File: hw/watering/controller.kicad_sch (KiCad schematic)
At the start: 10 parts, among them U1 ESP32-C6, Y1 40MHz

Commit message: updated power
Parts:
- removed C3: 4u7, Capacitor_SMD:C_0603_1608Metric, symbol Device:C
- added C5, C6, C7, C8: 100n, Capacitor_SMD:C_0603_1608Metric, symbol Device:C
- added SW1, SW2: KMS221GLFS, Button_Switch_SMD:SW_SPST_CK_KMS2xxGP, symbol Switch:SW_Push
- added Y2: 32768Hz, Crystal:Crystal_SMD_3215-2Pin_3.2x1.5mm, symbol Device:Crystal
- AE1: footprint (none) -> RF_Antenna:Texas_SWRA117D_2.4GHz_Left
- C4: value 4u7 -> 100n
- R7, R8: value 5k1 -> 10k
- Y1: footprint (none) -> Crystal:Crystal_SMD_3225-4Pin_3.2x2.5mm
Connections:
- net +3V3: now also C5.1, C6.1, C7.1, C8.1
- net GND: now also C5.2, C6.2, C7.2, C8.2, SW1.1, SW2.1
- net reset: now reaches U1.4 (CHIP_PU)
- net reset: now also SW1.2
- net boot: now reaches U1.6 (GPIO0/XTAL_32K_P/ADC1_CH0)
- net boot: now also SW2.2, Y2.1
- net at U1.7 (GPIO1/XTAL_32K_N/ADC1_CH1): now also Y2.2

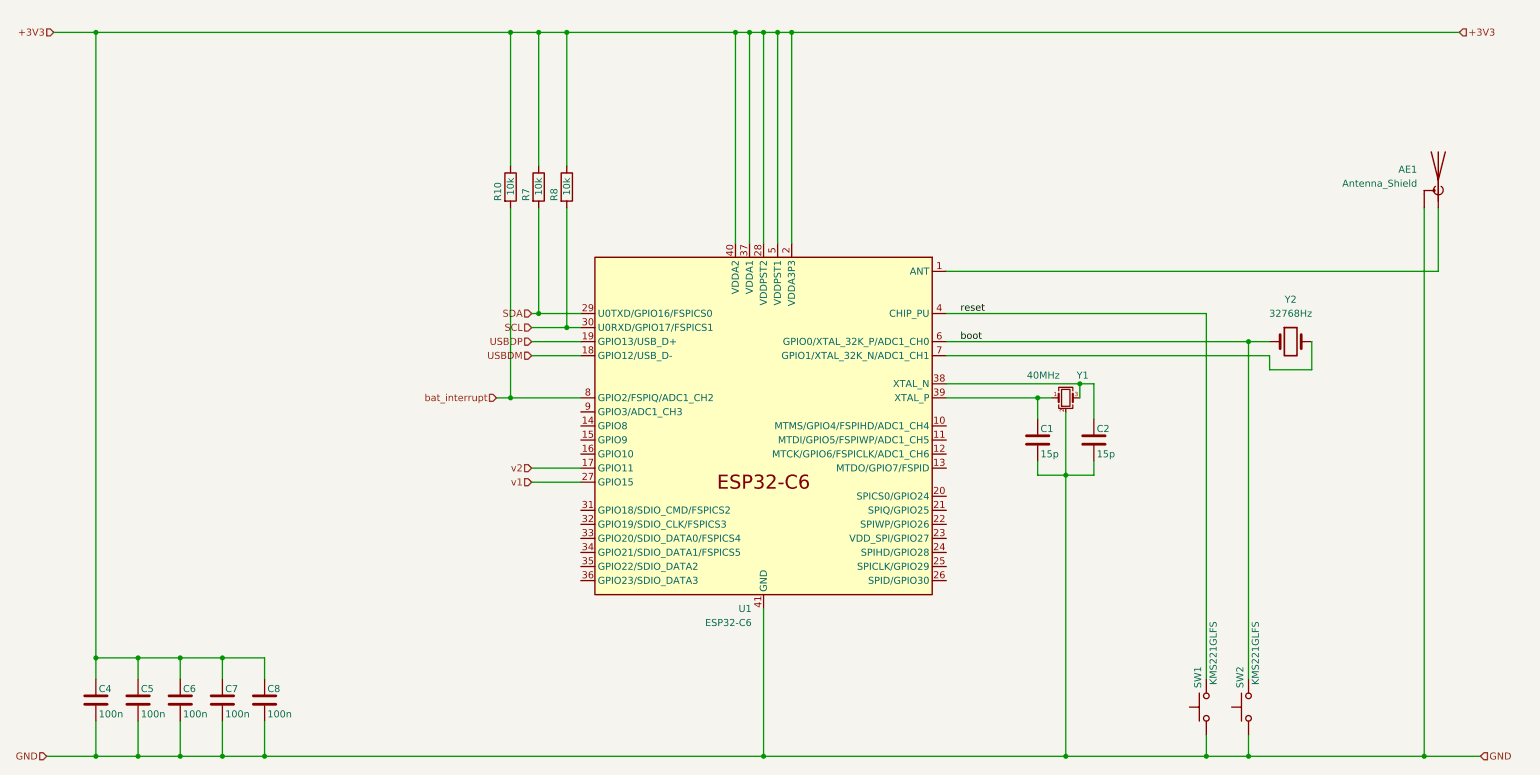
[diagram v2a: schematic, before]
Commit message: connections completet. started placing and routing
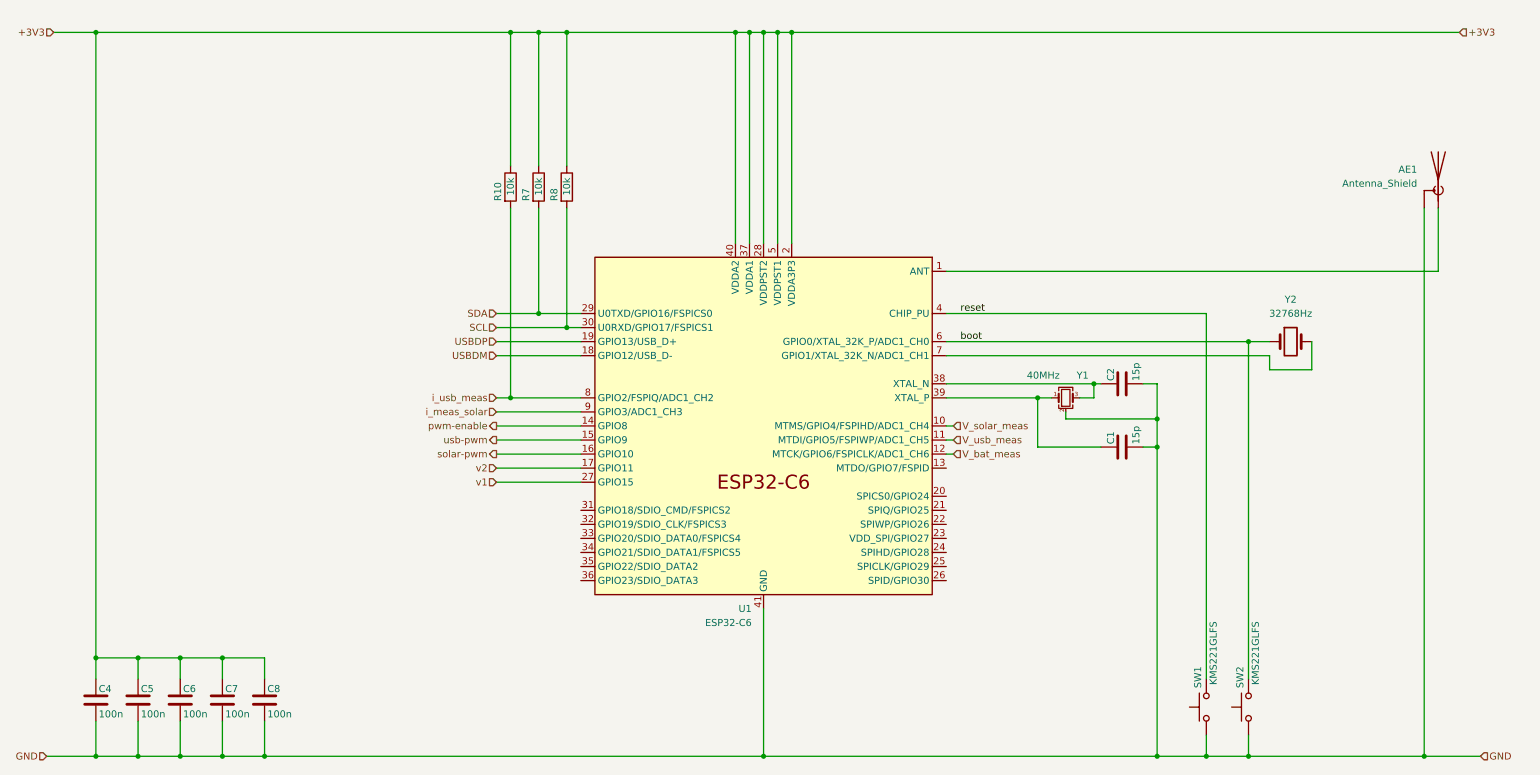
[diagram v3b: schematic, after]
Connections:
- net V_solar_meas: now reaches U1.10 (MTMS/GPIO4/FSPIHD/ADC1_CH4)
- net V_usb_meas: now reaches U1.11 (MTDI/GPIO5/FSPIWP/ADC1_CH5)
- net V_bat_meas: now reaches U1.12 (MTCK/GPIO6/FSPICLK/ADC1_CH6)
- net pwm-enable: now reaches U1.14 (GPIO8)
- net usb-pwm: now reaches U1.15 (GPIO9)
- net solar-pwm: now reaches U1.16 (GPIO10)
- net i_meas_solar: now reaches U1.9 (GPIO3/ADC1_CH3)
- net bat_interrupt renamed i_usb_meas
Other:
- moved on the sheet: C1, C2

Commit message: some more placing
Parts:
- removed C8: 100n, Capacitor_SMD:C_0603_1608Metric, symbol Device:C
- removed R7, R8: 10k, Resistor_SMD:R_0603_1608Metric, symbol Device:R

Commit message: routing done
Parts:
- removed C4: 100n, Capacitor_SMD:C_0603_1608Metric, symbol Device:C
- added C20: 1u, Capacitor_SMD:C_0603_1608Metric, symbol Device:C
- added R14, R31, R32, R35: 10k, Resistor_SMD:R_0603_1608Metric, symbol Device:R
- added R33, R34: 47, Resistor_SMD:R_0603_1608Metric, symbol Device:R
- added U3: W25Q128JVS, Package_SO:SOIC-8_5.3x5.3mm_P1.27mm, symbol Memory_Flash:W25Q128JVS
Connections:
- net +3V3: now also R14.1, R31.1, R32.1, R35.1
- net GND: now also C20.2, U3.4 (GND)
- net SCL: now also R32.2
- net SDA: now also R10.2
- net USBDM: now also R34.1; no longer U1.18 (GPIO12/USB_D-)
- net USBDP: now also R33.1; no longer U1.19 (GPIO13/USB_D+)
- net boot: now also U1.15 (GPIO9), R31.2; no longer U1.6 (GPIO0/XTAL_32K_P/ADC1_CH0), Y2.1
- net i_usb_meas: no longer R10.2
- net pwm-enable: now also U1.32 (GPIO19/SDIO_CLK/FSPICS3); no longer U1.14 (GPIO8)
- net reset: now also C20.1, R14.2
- net solar-pwm: now also U1.33 (GPIO20/SDIO_DATA0/FSPICS4); no longer U1.16 (GPIO10)
- net usb-pwm: now also U1.31 (GPIO18/SDIO_CMD/FSPICS2); no longer U1.15 (GPIO9)
- net antenna: now reaches AE1.1 (A), U1.1 (ANT)
- net at U1.20 (SPICS0/GPIO24): now also U3.1 (~{CS})
- net at U1.21 (SPIQ/GPIO25): now also U3.2 (DO/IO_{1})
- net at U1.22 (SPIWP/GPIO26): now also U3.3 (~{WP}/IO_{2})
- net at U1.23 (VDD_SPI/GPIO27): now also U3.8 (VCC)
- net at U1.24 (SPIHD/GPIO28): now also U3.7 (~{HOLD}/~{RESET}/IO_{3})
- net at U1.25 (SPICLK/GPIO29): now also U3.6 (CLK)
- net at U1.26 (SPID/GPIO30): now also U3.5 (DI/IO_{0})
- net V_usb_avail: now reaches U1.34 (GPIO21/SDIO_DATA1/FSPICS5)
- net cond_pwm: now reaches U1.35 (GPIO22/SDIO_DATA2)
- net cond_en: now reaches U1.36 (GPIO23/SDIO_DATA3)
- net V_usb_meas renamed i_cond_meas
- new net: R33.2, U1.19 (GPIO13/USB_D+)
- new net: R34.2, U1.18 (GPIO12/USB_D-)
- new net: R35.2, U1.14 (GPIO8)
- new net: U1.6 (GPIO0/XTAL_32K_P/ADC1_CH0), Y2.1
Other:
- moved on the sheet: AE1, C7, SW2

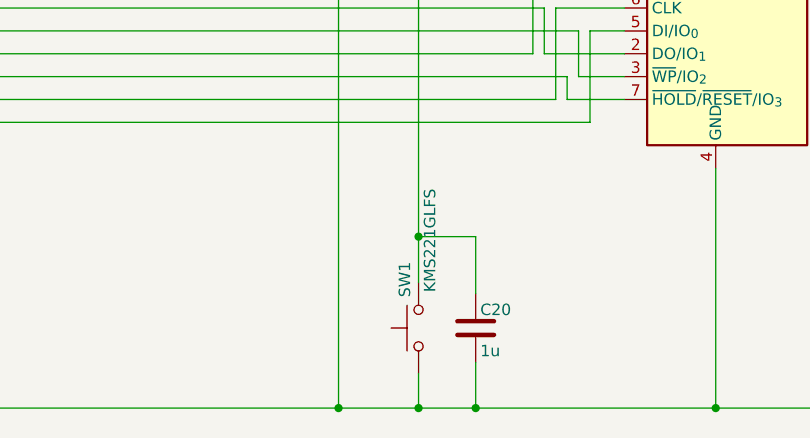
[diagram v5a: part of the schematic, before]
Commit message: updated switches
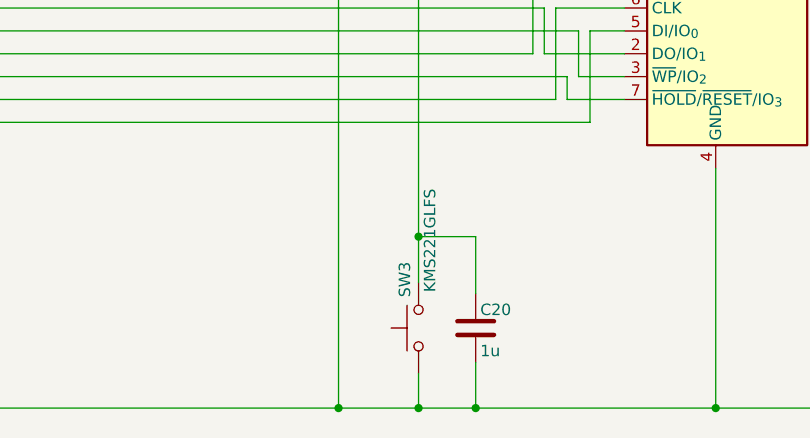
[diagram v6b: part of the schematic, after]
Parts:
- removed SW1: KMS221GLFS, Button_Switch_SMD:SW_SPST_CK_KMS2xxGP, symbol Switch:SW_Push
- added SW3: KMS221GLFS, Button_Switch_SMD:SW_SPST_TS-1088-xR020, symbol Switch:SW_Push
- SW2: footprint Button_Switch_SMD:SW_SPST_CK_KMS2xxGP -> Button_Switch_SMD:SW_SPST_TS-1088-xR020
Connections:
- net GND: now also SW3.1
- net reset: now also SW3.2
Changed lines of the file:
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@@
+	)
+	(symbol
+		(lib_id "Switch:SW_Push")
+		(at 228.6 143.51 90)
+		(unit 1)
+		(body_style 1)
+		(exclude_from_sim no)
+		(in_bom yes)
+		(on_board yes)
+		(in_pos_files yes)
+		(dnp no)
+		(property "Reference" "SW3"
+			(at 227.076 136.144 0)
+			(show_name no)
+			(do_not_autoplace no)
+			(effects
+				(font
+					(size 1.27 1.27)
+				)
+				(justify right)
+			)
+		)
+		(property "Value" "KMS221GLFS"
+			(at 229.87 128.016 0)
+			(show_name no)
+			(do_not_autoplace no)
+			(effects
+				(font
+					(size 1.27 1.27)
+				)
+				(justify right)
+			)
+		)
+		(property "Footprint" "Button_Switch_SMD:SW_SPST_TS-1088-xR020"
+			(at 223.52 143.51 0)
+			(hide yes)
+			(show_name no)
+			(do_not_autoplace no)
+			(effects
+				(font
+					(size 1.27 1.27)
+				)
+			)
+		)
+		(property "Datasheet" "https://jlc-prod-smt.oss-eu-central-1.aliyuncs.com/smtDataManualFile/8588903737833873408-C221698.pdf?response-content-disposition=attachment%3B%20filename%3DC221698.pdf%3B%20filename%2A%3DUTF-8%27%27C221698.pdf&x-oss-date=20260604T163458Z&x-oss-expires=1800&x-oss-security-token=CAISgAN1q6Ft5B2yfSjIr5rgEov%2B1Z5Y5IPeVHLE03MEOcpBm6iagzz2IHhMdHJsAOodtv0%2FmmhT6PkclqRLcbhpcmfjV%2BZHzLB8qaJ7%2B39A4J7b16cNrbH4M4H6aXeirtuwDsz9SNTCALjPD3nPii50x5bjaDymRCbLGJaViJlhHLN1Ow6jdmhpCctxLAlvo9NgFxm3D%2Fu2NQPwiWf9FVdhvhEG6Vly8qOi2MaRmFy8yFTx0b0SvJ%2BjYMrmPctoN9JnSdC5mfdzau3a1TJ84gRD0a5wkaVA1zbDs5bfISEIuUzebreLqY03dV4mOvdqIcMe8qigz88fk%2FfIioH6xyxKOexoSCnFTOiiupCcQLPyao9jLu6iayqViY7QaIOTqQohZmkAMwVOasAsI3Ngh4zF97Qt0cVNkXO9gWfLI8DtuMleWsrkxPosAnSgc5lCkRRYwGs1287ugXlSQzo890KPDAEovaKCnZ2ZSfh7Y4sNknI6i%2Bfc2Se2MIkIBfjYxKKWD5sagAGJZBLg4dXI2cxwZhpjHr9vfG2bcnPeD2ZekO6CLDE470zoyla87k22%2FMfMgD7nSJvKHKZxx7wRTJR2C%2FIed5gUddUWOOyzyialMQCX42pgq2cGFbW2xRzddJF8rKP5p2z7HTq0AIZLZQQExEqwnA3Me1xxudMxwbz09i63yKlbRSAA&x-oss-signature-version=OSS4-HMAC-SHA256&x-oss-credential=STS.NYUY1J8AySA5VTu7sQ5Emtm1a%2F20260604%2Feu-central-1%2Foss%2Faliyun_v4_request&x-oss-signature=0287d07f1d74dc173e35fdd16bbbdb40a7eb09e1df544025205ab3d6ea2886b8"
+			(at 223.52 143.51 0)
+			(hide yes)
+			(show_name no)
+			(do_not_autoplace no)
+			(effects
+				(font
+					(size 1.27 1.27)
+				)
+			)
+		)
+		(property "Description" "C720477"
+			(at 228.6 143.51 0)
+			(hide yes)
+			(show_name no)
+			(do_not_autoplace no)
+			(effects
+				(font
+					(size 1.27 1.27)
+				)
+			)
+		)
+		(pin "1"
+		)
+		(pin "2"
+		)
+		(instances
+			(project "watering"
+				(path "/cfeeaa6f-be25-403f-b03c-39be367d5a74/16cf7c18-cb1d-41f0-89f2-0e82671466a1"
+					(reference "SW3")
+					(unit 1)
+				)
+			)
+		)
 	)
 	(symbol
@@
 			)
 		)
-		(property "Footprint" "Button_Switch_SMD:SW_SPST_CK_KMS2xxGP"
+		(property "Footprint" "Button_Switch_SMD:SW_SPST_TS-1088-xR020"
 			(at 102.87 142.24 0)
 			(hide yes)
@@
 			)
 		)
-		(property "Description" "C221698"
+		(property "Description" "C720477"
 			(at 107.95 142.24 0)
 			(hide yes)
@@
 					(unit 1)
 				)
-			)
-		)
-	)
-	(symbol
-		(lib_id "Switch:SW_Push")
-		(at 228.6 143.51 90)
-		(unit 1)
-		(body_style 1)
-		(exclude_from_sim no)
-		(in_bom yes)
-		(on_board yes)
-		(in_pos_files yes)
-		(dnp no)
-		(property "Reference" "SW1"
-			(at 227.076 136.144 0)
-			(show_name no)
-			(do_not_autoplace no)
-			(effects
-				(font
-					(size 1.27 1.27)
-				)
-				(justify right)
-			)
-		)
-		(property "Value" "KMS221GLFS"
-			(at 229.87 128.016 0)
-			(show_name no)
-			(do_not_autoplace no)
-			(effects
-				(font
-					(size 1.27 1.27)
-				)
-				(justify right)
-			)
-		)
-		(property "Footprint" "Button_Switch_SMD:SW_SPST_CK_KMS2xxGP"
-			(at 223.52 143.51 0)
-			(hide yes)
-			(show_name no)
-			(do_not_autoplace no)
-			(effects
-				(font
-					(size 1.27 1.27)
-				)
-			)
-		)
-		(property "Datasheet" "https://jlc-prod-smt.oss-eu-central-1.aliyuncs.com/smtDataManualFile/8588903737833873408-C221698.pdf?response-content-disposition=attachment%3B%20filename%3DC221698.pdf%3B%20filename%2A%3DUTF-8%27%27C221698.pdf&x-oss-date=20260604T163458Z&x-oss-expires=1800&x-oss-security-token=CAISgAN1q6Ft5B2yfSjIr5rgEov%2B1Z5Y5IPeVHLE03MEOcpBm6iagzz2IHhMdHJsAOodtv0%2FmmhT6PkclqRLcbhpcmfjV%2BZHzLB8qaJ7%2B39A4J7b16cNrbH4M4H6aXeirtuwDsz9SNTCALjPD3nPii50x5bjaDymRCbLGJaViJlhHLN1Ow6jdmhpCctxLAlvo9NgFxm3D%2Fu2NQPwiWf9FVdhvhEG6Vly8qOi2MaRmFy8yFTx0b0SvJ%2BjYMrmPctoN9JnSdC5mfdzau3a1TJ84gRD0a5wkaVA1zbDs5bfISEIuUzebreLqY03dV4mOvdqIcMe8qigz88fk%2FfIioH6xyxKOexoSCnFTOiiupCcQLPyao9jLu6iayqViY7QaIOTqQohZmkAMwVOasAsI3Ngh4zF97Qt0cVNkXO9gWfLI8DtuMleWsrkxPosAnSgc5lCkRRYwGs1287ugXlSQzo890KPDAEovaKCnZ2ZSfh7Y4sNknI6i%2Bfc2Se2MIkIBfjYxKKWD5sagAGJZBLg4dXI2cxwZhpjHr9vfG2bcnPeD2ZekO6CLDE470zoyla87k22%2FMfMgD7nSJvKHKZxx7wRTJR2C%2FIed5gUddUWOOyzyialMQCX42pgq2cGFbW2xRzddJF8rKP5p2z7HTq0AIZLZQQExEqwnA3Me1xxudMxwbz09i63yKlbRSAA&x-oss-signature-version=OSS4-HMAC-SHA256&x-oss-credential=STS.NYUY1J8AySA5VTu7sQ5Emtm1a%2F20260604%2Feu-central-1%2Foss%2Faliyun_v4_request&x-oss-signature=0287d07f1d74dc173e35fdd16bbbdb40a7eb09e1df544025205ab3d6ea2886b8"
-			(at 223.52 143.51 0)
-			(hide yes)
-			(show_name no)
-			(do_not_autoplace no)
-			(effects
-				(font
-					(size 1.27 1.27)
-				)
-			)
-		)
-		(property "Description" "C221698"
-			(at 228.6 143.51 0)
-			(hide yes)
-			(show_name no)
-			(do_not_autoplace no)
-			(effects
-				(font
-					(size 1.27 1.27)
-				)
-			)
-		)
-		(pin "1"
-		)
-		(pin "2"
-		)
-		(instances
-			(project "watering"
-				(path "/cfeeaa6f-be25-403f-b03c-39be367d5a74/16cf7c18-cb1d-41f0-89f2-0e82671466a1"
-					(reference "SW1")
-					(unit 1)
-				)
